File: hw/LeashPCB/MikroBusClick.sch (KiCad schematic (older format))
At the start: 2 parts, among them J701 mikroBUS, J702 mikroBUS

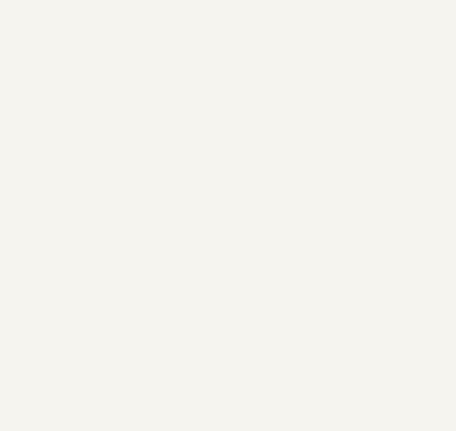
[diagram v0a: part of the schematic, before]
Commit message: Connected up some of the top level power signals
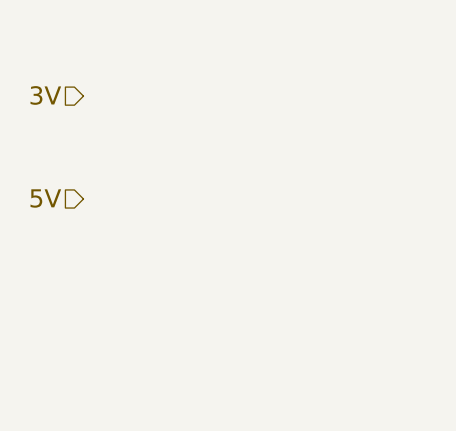
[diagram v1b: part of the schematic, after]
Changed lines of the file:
@@
 	1    0    0    -1
 $EndComp
+Text HLabel 3025 2775 0    79   Input ~ 0
+3V
+Text HLabel 3025 3225 0    79   Input ~ 0
+5V
 $EndSCHEMATC

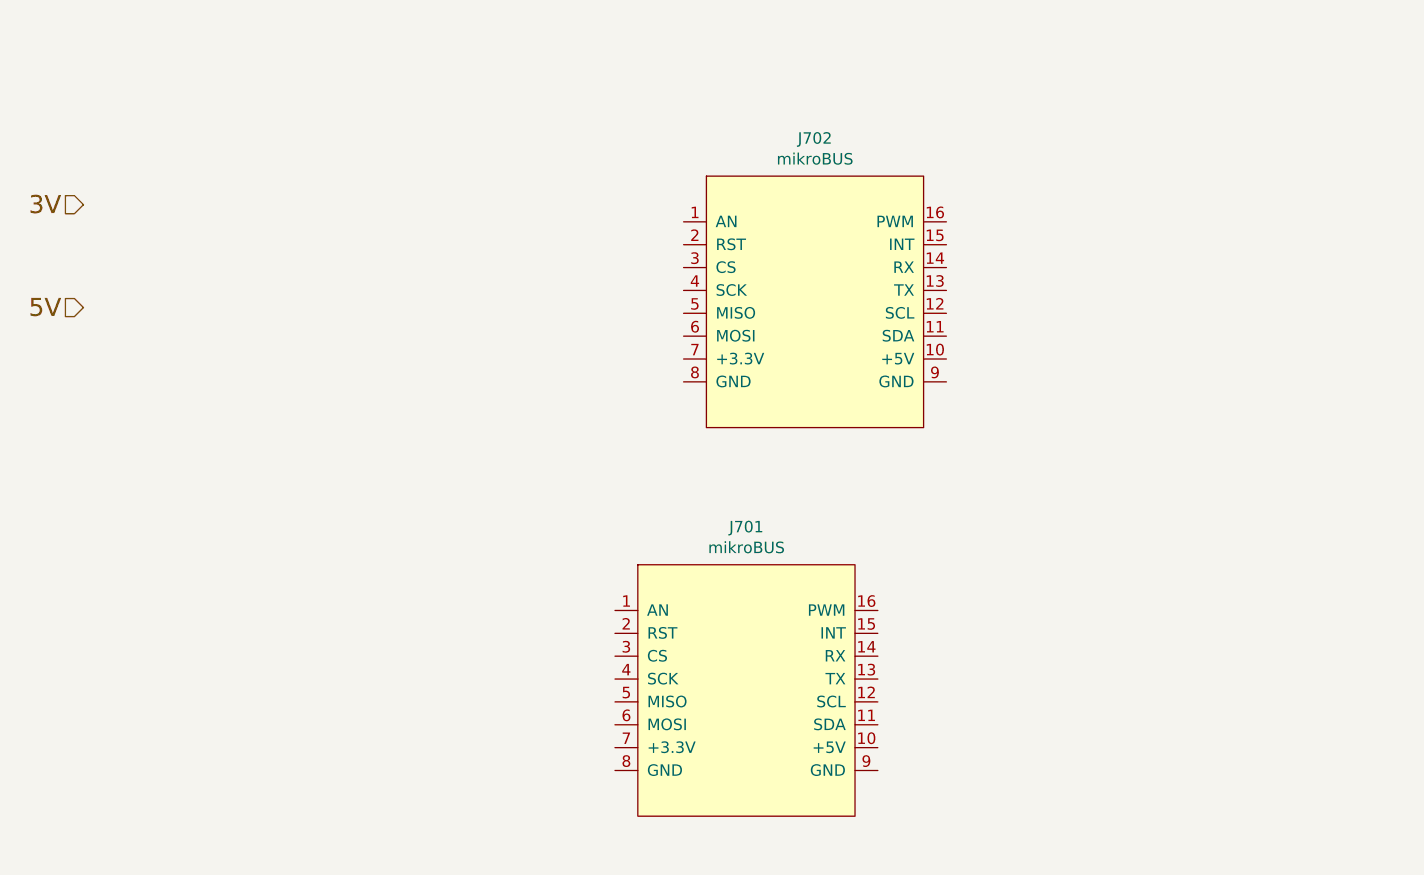
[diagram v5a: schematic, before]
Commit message: Shifted all components to the left on the layout and added passives
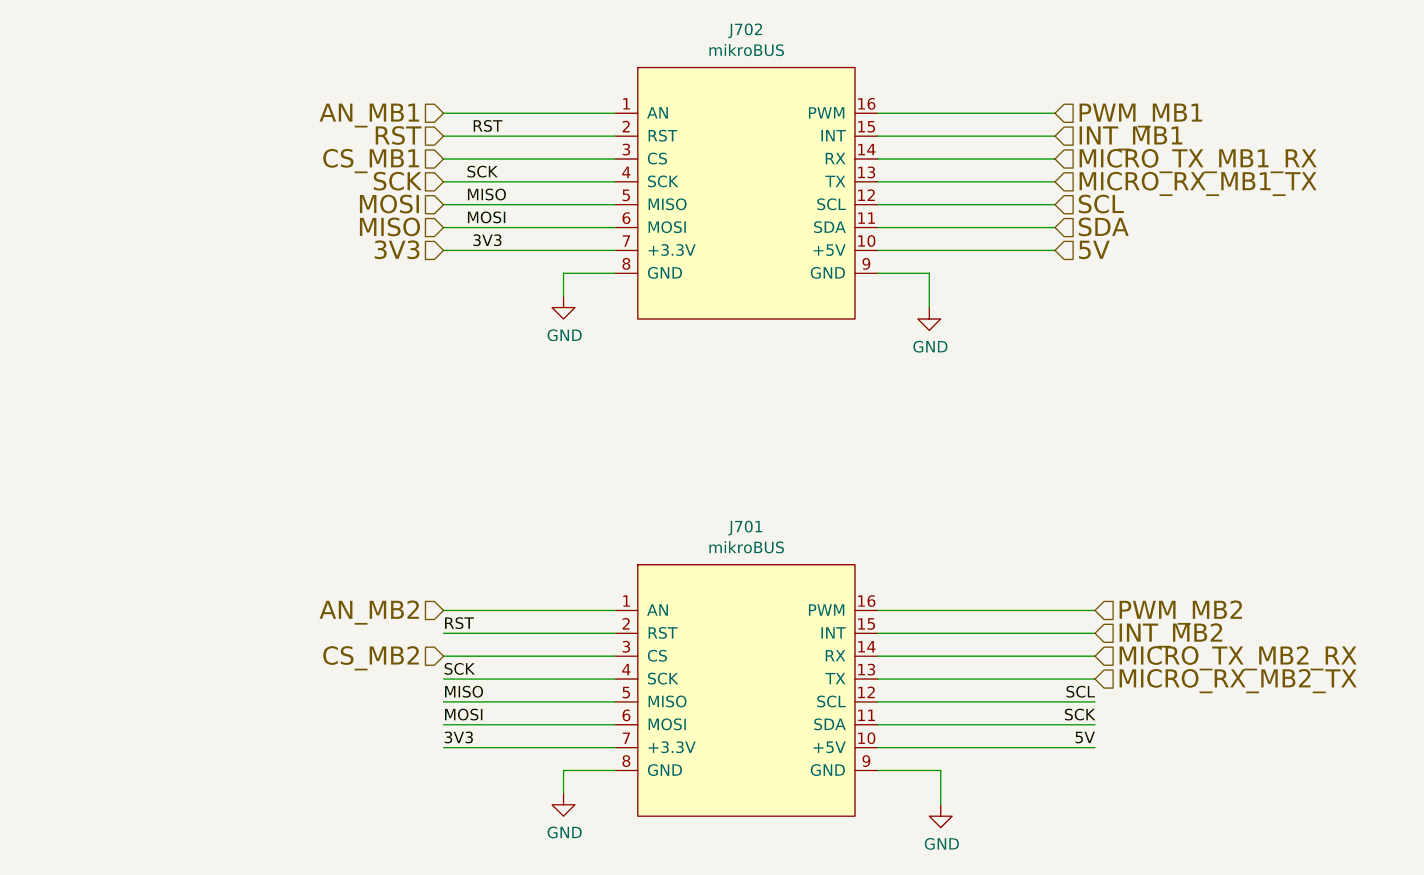
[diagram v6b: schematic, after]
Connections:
- net 5V: now also J701.10 (+5V), J702.10 (+5V)
- net AN_MB1: now reaches J702.1 (AN)
- net SDA: now reaches J702.11 (SDA)
- net SCL: now reaches J702.12 (SCL)
- net SCL: now also J701.12 (SCL)
- net MICRO_RX_MB1_TX: now reaches J702.13 (TX)
- net MICRO_TX_MB1_RX: now reaches J702.14 (RX)
- net INT_MB1: now reaches J702.15 (INT)
- net PWM_MB1: now reaches J702.16 (PWM)
- net RST: now reaches J702.2 (RST)
- net RST: now also J701.2 (RST)
- net CS_MB1: now reaches J702.3 (CS)
- net SCK: now reaches J702.4 (SCK)
- net SCK: now also J701.11 (SDA), J701.4 (SCK)
- net MISO: now reaches J702.5 (MISO)
- net MISO: now also J701.5 (MISO), J701.6 (MOSI), J702.6 (MOSI)
- net 3V3: now reaches J702.7 (+3.3V)
- net 3V3: now also J701.7 (+3.3V)
- net GND: now reaches J702.8 (GND)
- net GND: now also J701.8 (GND), J701.9 (GND), J702.9 (GND)
- net AN_MB2: now reaches J701.1 (AN)
- net MICRO_RX_MB2_TX: now reaches J701.13 (TX)
- net MICRO_TX_MB2_RX: now reaches J701.14 (RX)
- net INT_MB2: now reaches J701.15 (INT)
- net PWM_MB2: now reaches J701.16 (PWM)
- net CS_MB2: now reaches J701.3 (CS)
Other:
- moved on the sheet: J702
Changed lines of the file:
@@
 $Descr A4 11693 8268
 encoding utf-8
-Sheet 7 10
+Sheet 6 10
 Title ""
 Date ""
@@
 L LeashPCB:mikroBUS J?
 U 1 1 5D092D9C
-P 6200 3200
+P 5900 2725
 AR Path="/5D092D9C" Ref="J?"  Part="1"
 AR Path="/5D066680/5D092D9C" Ref="J702"  Part="1"
-F 0 "J702" H 6225 3915 50  0000 C CNN
-F 1 "mikroBUS" H 6225 3824 50  0000 C CNN
-F 2 "leash:MikroBus-SMD" H 6000 3400 50  0001 C CNN
-F 3 "" H 6000 3400 50  0001 C CNN
-F 4 "0" H 6200 3200 50  0001 C CNN "Standard Price"
-	1    6200 3200
+F 0 "J702" H 5925 3440 50  0000 C CNN
+F 1 "mikroBUS" H 5925 3349 50  0000 C CNN
+F 2 "leash:MikroBus-SMD" H 5700 2925 50  0001 C CNN
+F 3 "" H 5700 2925 50  0001 C CNN
+F 4 "0" H 5900 2725 50  0001 C CNN "Standard Price"
+	1    5900 2725
 	1    0    0    -1
 $EndComp
@@
 	1    0    0    -1
 $EndComp
-Text HLabel 3025 2775 0    79   Input ~ 0
-3V
-Text HLabel 3025 3225 0    79   Input ~ 0
+Text HLabel 4600 2975 0    79   Input ~ 0
+3V3
+Text HLabel 7275 2975 2    79   Input ~ 0
+5V
+Text HLabel 4600 2375 0    79   Input ~ 0
+AN_MB1
+Text HLabel 4600 2475 0    79   Input ~ 0
+RST
+Text HLabel 4600 2575 0    79   Input ~ 0
+CS_MB1
+Text HLabel 4600 4750 0    79   Input ~ 0
+CS_MB2
+Text HLabel 4600 2675 0    79   Input ~ 0
+SCK
+Text HLabel 4600 2875 0    79   Input ~ 0
+MISO
+Text HLabel 4600 2775 0    79   Input ~ 0
+MOSI
+Text HLabel 7275 2375 2    79   Input ~ 0
+PWM_MB1
+Text HLabel 7450 4550 2    79   Input ~ 0
+PWM_MB2
+Text HLabel 7275 2475 2    79   Input ~ 0
+INT_MB1
+Text HLabel 7450 4650 2    79   Input ~ 0
+INT_MB2
+Text HLabel 7275 2575 2    79   Input ~ 0
+MICRO_TX_MB1_RX
+Text HLabel 7450 4750 2    79   Input ~ 0
+MICRO_TX_MB2_RX
+Text HLabel 7275 2675 2    79   Input ~ 0
+MICRO_RX_MB1_TX
+Text HLabel 7450 4850 2    79   Input ~ 0
+MICRO_RX_MB2_TX
+Text HLabel 7275 2875 2    79   Input ~ 0
+SDA
+Wire Wire Line
+	5350 2975 4600 2975
+Wire Wire Line
+	5350 3075 5125 3075
+Wire Wire Line
+	5125 3075 5125 3175
+$Comp
+L power:GND #PWR0104
+U 1 1 5D1F9F78
+P 5125 3175
+F 0 "#PWR0104" H 5125 2925 50  0001 C CNN
+F 1 "GND" H 5130 3002 50  0000 C CNN
+F 2 "" H 5125 3175 50  0001 C CNN
+F 3 "" H 5125 3175 50  0001 C CNN
+	1    5125 3175
+	1    0    0    -1
+$EndComp
+Wire Wire Line
+	4600 2875 5350 2875
+Wire Wire Line
+	4600 2775 5350 2775
+Wire Wire Line
+	4600 2675 5350 2675
+Wire Wire Line
+	4600 2375 5350 2375
+Wire Wire Line
+	5350 2475 4600 2475
+Wire Wire Line
+	5350 2575 4600 2575
+Wire Wire Line
+	6500 2975 7275 2975
+$Comp
+L power:GND #PWR0105
+U 1 1 5D200D92
+P 6725 3225
+F 0 "#PWR0105" H 6725 2975 50  0001 C CNN
+F 1 "GND" H 6730 3052 50  0000 C CNN
+F 2 "" H 6725 3225 50  0001 C CNN
+F 3 "" H 6725 3225 50  0001 C CNN
+	1    6725 3225
+	1    0    0    -1
+$EndComp
+Wire Wire Line
+	6725 3075 6500 3075
+Wire Wire Line
+	6725 3075 6725 3225
+Text HLabel 7275 2775 2    79   Input ~ 0
+SCL
+Wire Wire Line
+	7275 2375 6500 2375
+Wire Wire Line
+	7275 2475 6500 2475
+Wire Wire Line
+	6500 2575 7275 2575
+Wire Wire Line
+	7275 2675 6500 2675
+Wire Wire Line
+	6500 2775 7275 2775
+Wire Wire Line
+	7275 2875 6500 2875
+Wire Wire Line
+	5350 4750 4600 4750
+Wire Wire Line
+	4600 4550 5350 4550
+Text HLabel 4600 4550 0    79   Input ~ 0
+AN_MB2
+Text Label 4725 2475 0    50   ~ 0
+RST
+Text Label 4600 4650 0    50   ~ 0
+RST
+Wire Wire Line
+	4600 4650 5350 4650
+Text Label 4700 2675 0    50   ~ 0
+SCK
+Text Label 4700 2775 0    50   ~ 0
+MISO
+Text Label 4700 2875 0    50   ~ 0
+MOSI
+Text Label 4725 2975 0    50   ~ 0
+3V3
+Wire Wire Line
+	5350 5150 4600 5150
+Wire Wire Line
+	4600 5050 5350 5050
+Wire Wire Line
+	4600 4950 5350 4950
+Wire Wire Line
+	4600 4850 5350 4850
+Text Label 4600 4850 0    50   ~ 0
+SCK
+Text Label 4600 4950 0    50   ~ 0
+MISO
+Text Label 4600 5050 0    50   ~ 0
+MOSI
+Text Label 4600 5150 0    50   ~ 0
+3V3
+Wire Wire Line
+	5350 5250 5125 5250
+Wire Wire Line
+	5125 5250 5125 5350
+$Comp
+L power:GND #PWR0106
+U 1 1 5D217A46
+P 5125 5350
+F 0 "#PWR0106" H 5125 5100 50  0001 C CNN
+F 1 "GND" H 5130 5177 50  0000 C CNN
+F 2 "" H 5125 5350 50  0001 C CNN
+F 3 "" H 5125 5350 50  0001 C CNN
+	1    5125 5350
+	1    0    0    -1
+$EndComp
+Wire Wire Line
+	6500 4550 7450 4550
+Wire Wire Line
+	7450 4650 6500 4650
+Wire Wire Line
+	6500 4750 7450 4750
+Wire Wire Line
+	7450 4850 6500 4850
+Wire Wire Line
+	6500 4950 7450 4950
+Wire Wire Line
+	6500 5050 7450 5050
+Wire Wire Line
+	6500 5150 7450 5150
+$Comp
+L power:GND #PWR0107
+U 1 1 5D220EE5
+P 6775 5400
+F 0 "#PWR0107" H 6775 5150 50  0001 C CNN
+F 1 "GND" H 6780 5227 50  0000 C CNN
+F 2 "" H 6775 5400 50  0001 C CNN
+F 3 "" H 6775 5400 50  0001 C CNN
+	1    6775 5400
+	1    0    0    -1
+$EndComp
+Wire Wire Line
+	6775 5250 6775 5400
+Wire Wire Line
+	6500 5250 6775 5250
+Text Label 7450 4950 2    50   ~ 0
+SCL
+Text Label 7450 5050 2    50   ~ 0
+SCK
+Text Label 7450 5150 2    50   ~ 0
 5V
 $EndSCHEMATC

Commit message: Hooked up top level signals between cc1352r and the click headers and imported footprints from passives added yesterday
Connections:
- net MISO: no longer J701.6 (MOSI), J702.6 (MOSI)
- new net MOSI: J701.6 (MOSI), J702.6 (MOSI)
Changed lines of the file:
@@
 $Descr A4 11693 8268
 encoding utf-8
-Sheet 6 10
+Sheet 9 10
 Title ""
 Date ""
@@
 Text HLabel 4600 2675 0    79   Input ~ 0
 SCK
+Text HLabel 4600 2775 0    79   Input ~ 0
+MISO
 Text HLabel 4600 2875 0    79   Input ~ 0
-MISO
-Text HLabel 4600 2775 0    79   Input ~ 0
 MOSI
 Text HLabel 7275 2375 2    79   Input ~ 0

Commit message: Added antenna and routed ideal diode circuit
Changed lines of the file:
@@
 EESchema Schematic File Version 4
-LIBS:LeashPCB-cache
 EELAYER 29 0
 EELAYER END
@@
 Text Label 7450 5150 2    50   ~ 0
 5V
+Text Label 7175 2975 2    50   ~ 0
+5V
 $EndSCHEMATC
